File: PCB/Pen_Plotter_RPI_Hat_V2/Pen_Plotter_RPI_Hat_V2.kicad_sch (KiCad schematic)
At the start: 8 parts, among them U1 ATmega328P-P, Y1 X322516MLB4SI

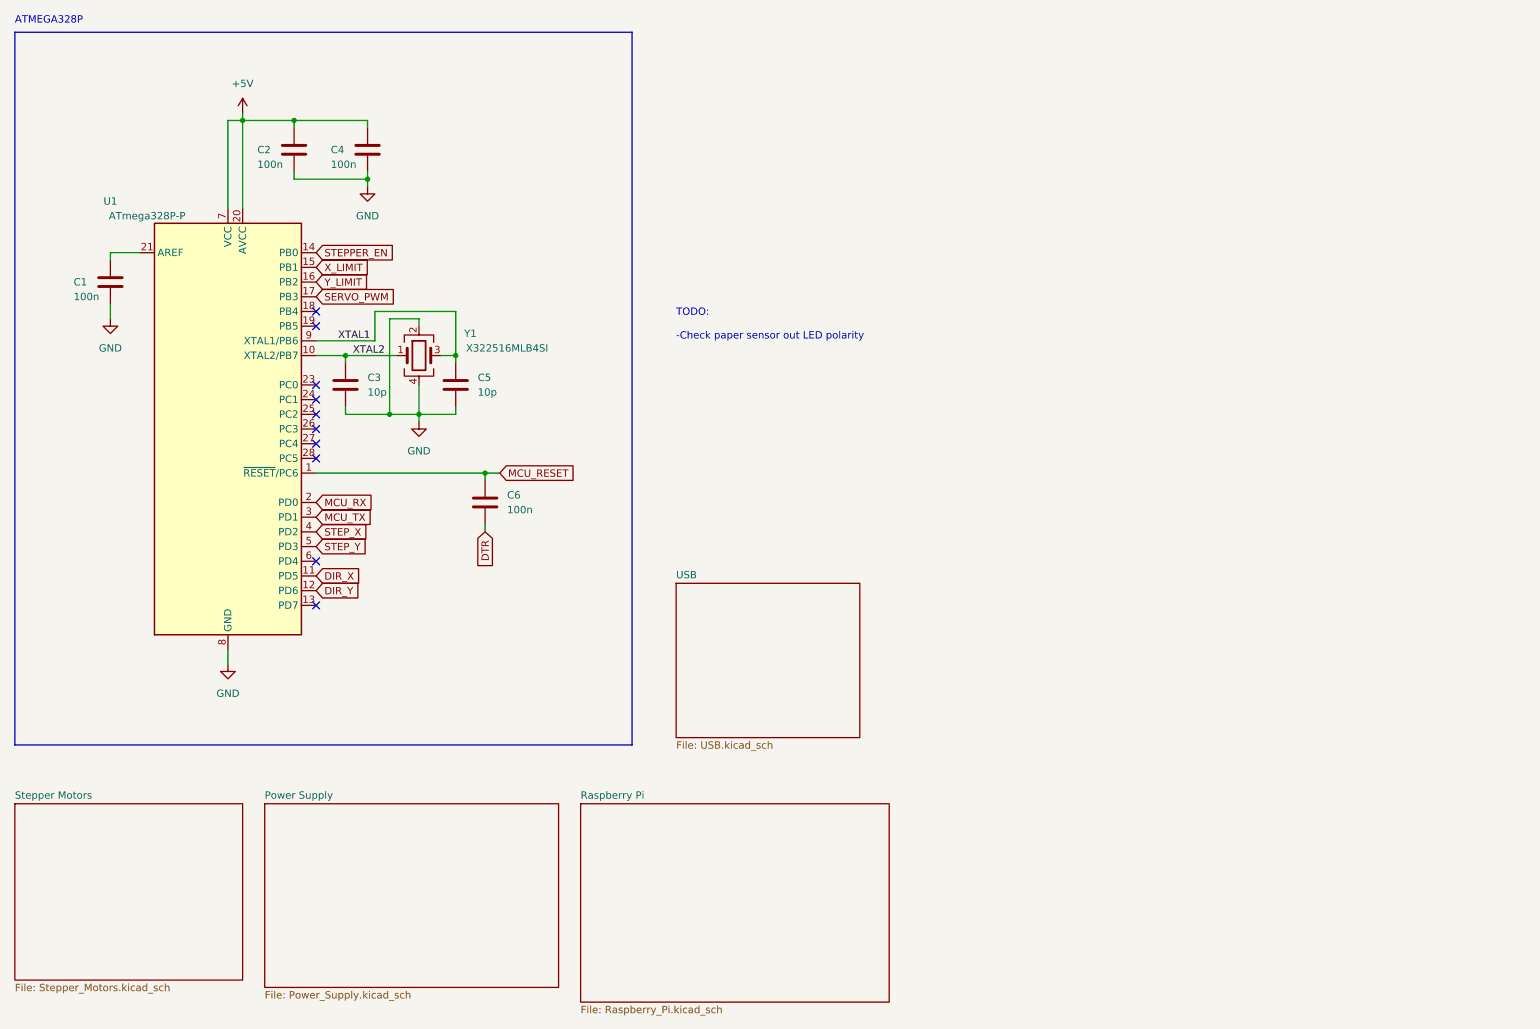
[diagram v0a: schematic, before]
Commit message: Simplified design, began layout process
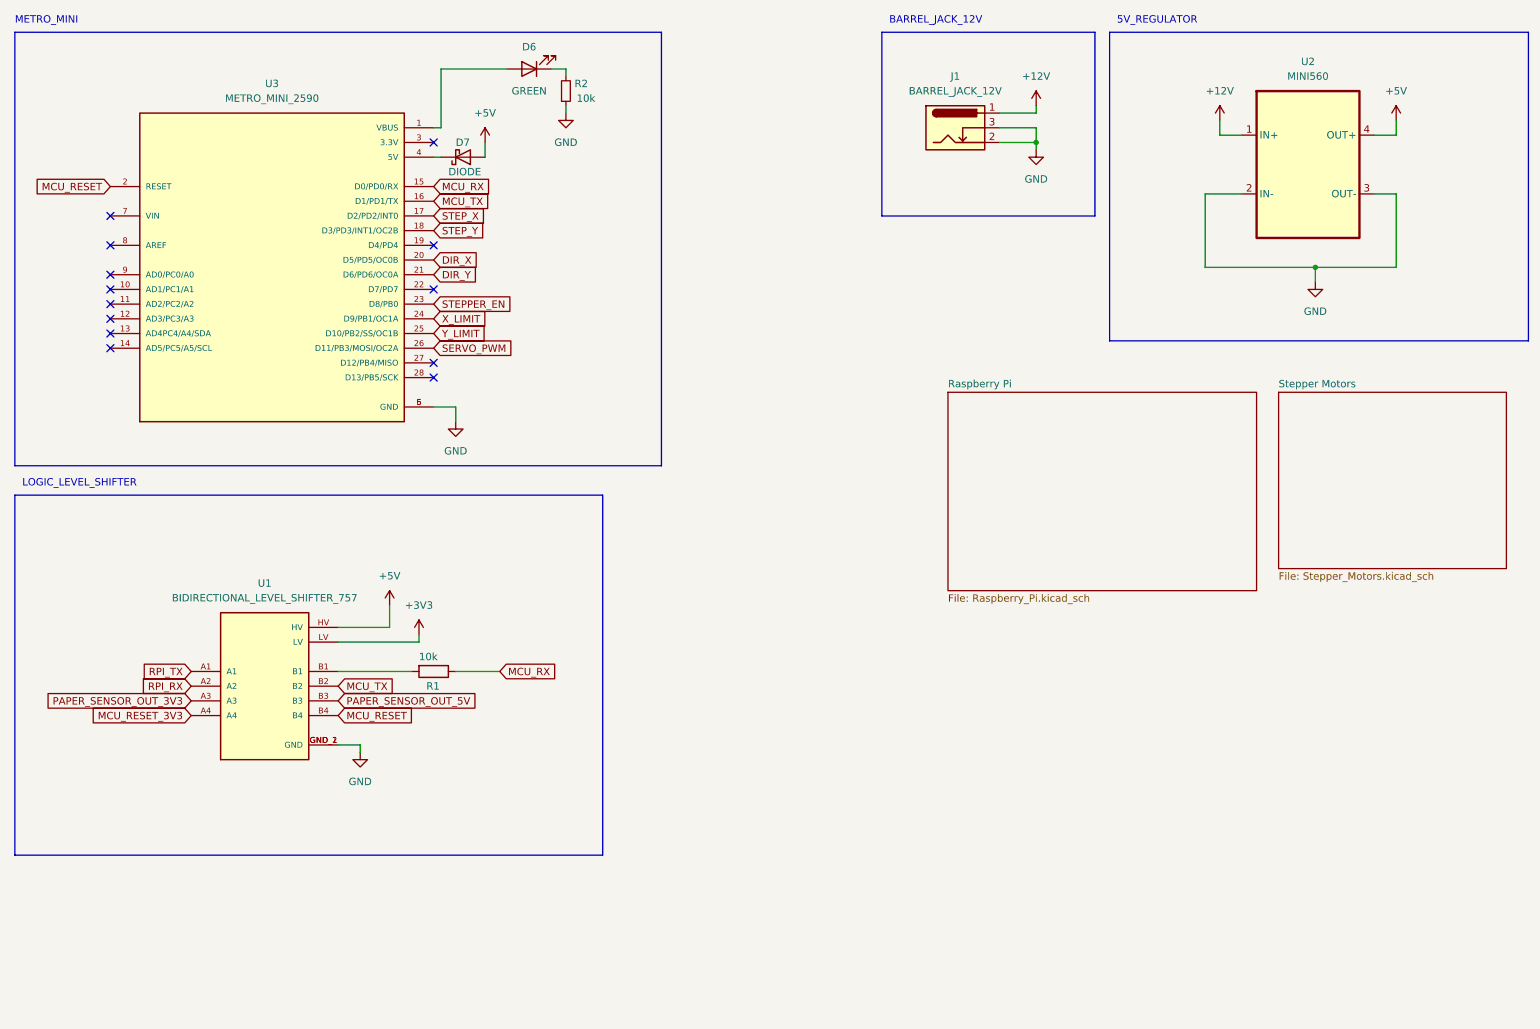
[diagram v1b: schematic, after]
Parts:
- removed C1, C2, C4, C6: 100n, Capacitor_SMD:C_0805_2012Metric, symbol Device:C
- removed C3, C5: 10p, Capacitor_SMD:C_0603_1608Metric, symbol Device:C
- removed U1: ATmega328P-P, Package_DIP:DIP-28_W7.62mm, symbol MCU_Microchip_ATmega:ATmega328P-P
- removed Y1: X322516MLB4SI, Crystal:Crystal_SMD_3225-4Pin_3.2x2.5mm, symbol Device:Crystal_GND24
- added D6: GREEN, LED_THT:LED_D5.0mm, symbol Device:LED
- added D7: DIODE, Diode_THT:D_5W_P10.16mm_Horizontal, symbol Device:D_Schottky
- added J1: BARREL_JACK_12V, Connector_BarrelJack:BarrelJack_Wuerth_6941xx301002, symbol Connector:Barrel_Jack_Switch
- added R1: 10k, Pen_Plotter_Lib:THT_RESISTOR_WITH_VALUE, symbol Device:R
- added R2: 10k, Pen_Plotter_Lib:THT_RESISTOR_WITH_VALUE, symbol Device:R_Small
- added U1: BIDIRECTIONAL_LEVEL_SHIFTER_757, Pen_Plotter_Lib:BIDIRECTIONAL_LEVEL_SHIFTER_575, symbol Pen_Plotter_Lib:BIDIRECTIONAL_LEVEL_SHIFTER_757
- added U2: MINI560, Pen_Plotter_Lib:MINI560_5V, symbol Pen_Plotter_Lib:MINI560
- added U3: METRO_MINI_2590, Pen_Plotter_Lib:METRO_MINI_MODULE_2590, symbol Pen_Plotter_Lib:METRO_MINI_2590
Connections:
- net +5V: now also D7.2 (A), U1.HV, U2.4 (OUT+)
- net DIR_X: now also U3.20 (D5/PD5/OC0B)
- net DIR_Y: now also U3.21 (D6/PD6/OC0A)
- net GND: now also J1.2, J1.3, R2.1, U1.GND_1 (GND), U1.GND_2 (GND), U2.2 (IN-), U2.3 (OUT-), U3.5 (GND), U3.6 (GND)
- net MCU_RESET: now also U1.B4, U3.2 (RESET)
- net MCU_RX: now also R1.1, U3.15 (D0/PD0/RX)
- net MCU_TX: now also U1.B2, U3.16 (D1/PD1/TX)
- net SERVO_PWM: now also U3.26 (D11/PB3/MOSI/OC2A)
- net STEPPER_EN: now also U3.23 (D8/PB0)
- net STEP_X: now also U3.17 (D2/PD2/INT0)
- net STEP_Y: now also U3.18 (D3/PD3/INT1/OC2B)
- net X_LIMIT: now also U3.24 (D9/PB1/OC1A)
- net Y_LIMIT: now also U3.25 (D10/PB2/SS/OC1B)
- new net: R1.2, U1.B1
- new net: D6.2 (A), U3.1 (VBUS)
- new net: D7.1 (K), U3.4 (5V)
- new net: D6.1 (K), R2.2
- new net +12V: J1.1, U2.1 (IN+)
- new net +3V3: U1.LV
- new net MCU_RESET_3V3: U1.A4
- new net PAPER_SENSOR_OUT_3V3: U1.A3
- new net PAPER_SENSOR_OUT_5V: U1.B3
- new net RPI_RX: U1.A2
- new net RPI_TX: U1.A1
- no-connect marks 10 -> 13
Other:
- removed sheet Power Supply
- removed sheet USB
- note added: "5V_REGULATOR"
- note added: "BARREL_JACK_12V"
- note added: "LOGIC_LEVEL_SHIFTER"
- note added: "METRO_MINI"
- note removed: "ATMEGA328P"
- note removed: "TODO: -Check paper sensor out LED polarity"

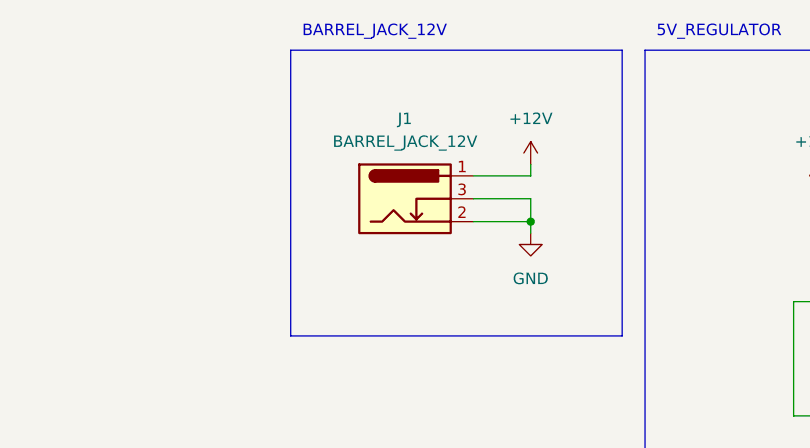
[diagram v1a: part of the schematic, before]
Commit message: Completed PCB layout, started routing
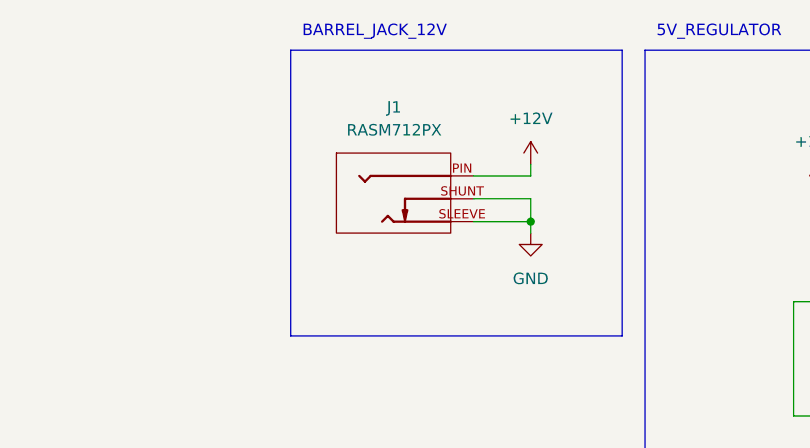
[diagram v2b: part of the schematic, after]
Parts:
- removed J1: BARREL_JACK_12V, Connector_BarrelJack:BarrelJack_Wuerth_6941xx301002, symbol Connector:Barrel_Jack_Switch
- added J1: RASM712PX, Pen_Plotter_Lib:SWITCHCRAFT_RASM712PX, symbol Pen_Plotter_Lib:RASM712PX
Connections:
- net +12V: now also J1.PIN
- net GND: now also J1.SHUNT, J1.SLEEVE
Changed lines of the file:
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@@
+    )
+  )
+  (symbol (lib_id "Pen_Plotter_Lib:RASM712PX") (at 181.61 39.37 0) (unit 1)
+    (in_bom yes) (on_board yes) (dnp no) (fields_autoplaced)
+    (property "Reference" "J1" (at 180.4035 29.21 0)
+      (effects (font (size 1.27 1.27)))
+    )
+    (property "Value" "RASM712PX" (at 180.4035 31.75 0)
+      (effects (font (size 1.27 1.27)))
+    )
+    (property "Footprint" "Pen_Plotter_Lib:SWITCHCRAFT_RASM712PX" (at 181.61 39.37 0)
+      (effects (font (size 1.27 1.27)) (justify bottom) hide)
+    )
+    (property "Datasheet" "" (at 181.61 39.37 0)
+      (effects (font (size 1.27 1.27)) hide)
+    )
+    (property "PARTREV" "A" (at 181.61 39.37 0)
+      (effects (font (size 1.27 1.27)) (justify bottom) hide)
+    )
+    (property "STANDARD" "Manufacturer Recommendations" (at 181.61 39.37 0)
+      (effects (font (size 1.27 1.27)) (justify bottom) hide)
+    )
+    (property "MAXIMUM_PACKAGE_HEIGHT" "11.11 mm" (at 181.61 39.37 0)
+      (effects (font (size 1.27 1.27)) (justify bottom) hide)
+    )
+    (property "MANUFACTURER" "Switchcraft" (at 181.61 39.37 0)
+      (effects (font (size 1.27 1.27)) (justify bottom) hide)
+    )
+    (pin "SLEEVE")
+    (pin "PIN")
+    (pin "SHUNT")
+    (instances
+      (project "Pen_Plotter_RPI_Hat_V2"
+        (path "/a2e71921-3692-4a11-8676-7b25cde44301"
+          (reference "J1") (unit 1)
+        )
+      )
     )
   )
@@
         )
       )
-    )
-  )
-  (symbol (lib_id "Connector:Barrel_Jack_Switch") (at 181.61 39.37 0) (unit 1)
-    (in_bom yes) (on_board yes) (dnp no) (fields_autoplaced)
-    (property "Reference" "J1" (at 181.61 30.48 0)
-      (effects (font (size 1.27 1.27)))
-    )
-    (property "Value" "BARREL_JACK_12V" (at 181.61 33.02 0)
-      (effects (font (size 1.27 1.27)))
-    )
-    (property "Footprint" "Connector_BarrelJack:BarrelJack_Wuerth_6941xx301002" (at 182.88 40.386 0)
-      (effects (font (size 1.27 1.27)) hide)
-    )
-    (property "Datasheet" "~" (at 182.88 40.386 0)
-      (effects (font (size 1.27 1.27)) hide)
-    )
-    (pin "1")
-    (pin "3")
-    (pin "2")
-    (instances
-      (project "Pen_Plotter_RPI_Hat_V2"
-        (path "/a2e71921-3692-4a11-8676-7b25cde44301"
-          (reference "J1") (unit 1)
-        )
-      )

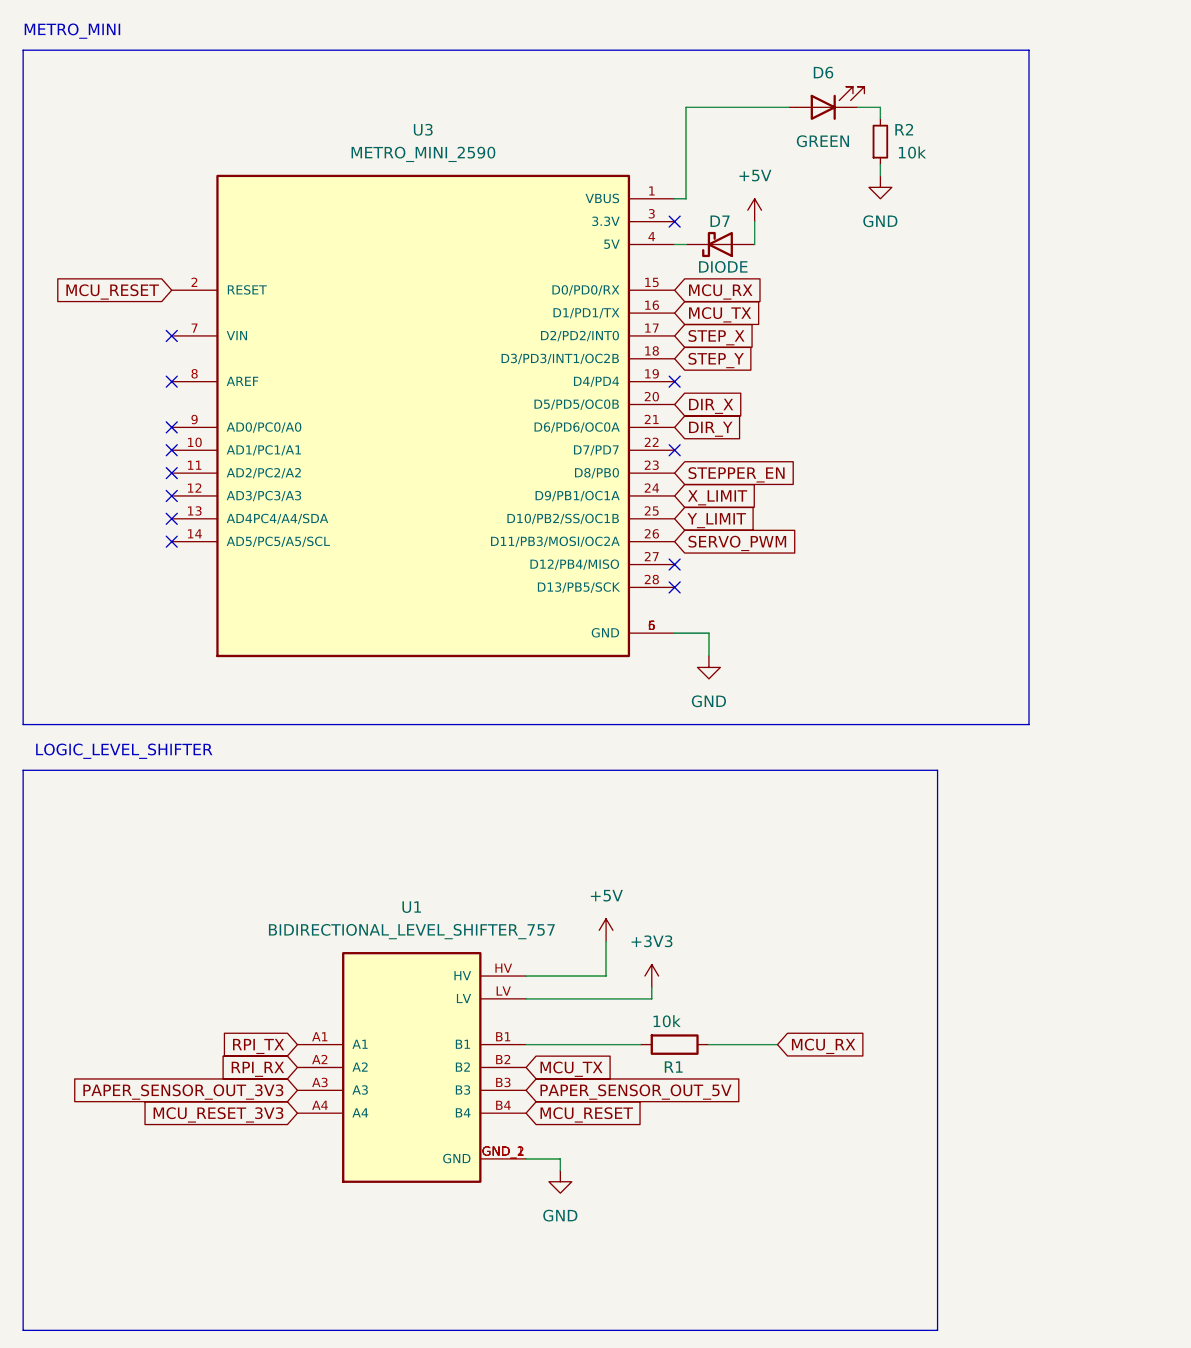
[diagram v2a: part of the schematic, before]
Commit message: Started work on converting to atmega328p control circuit
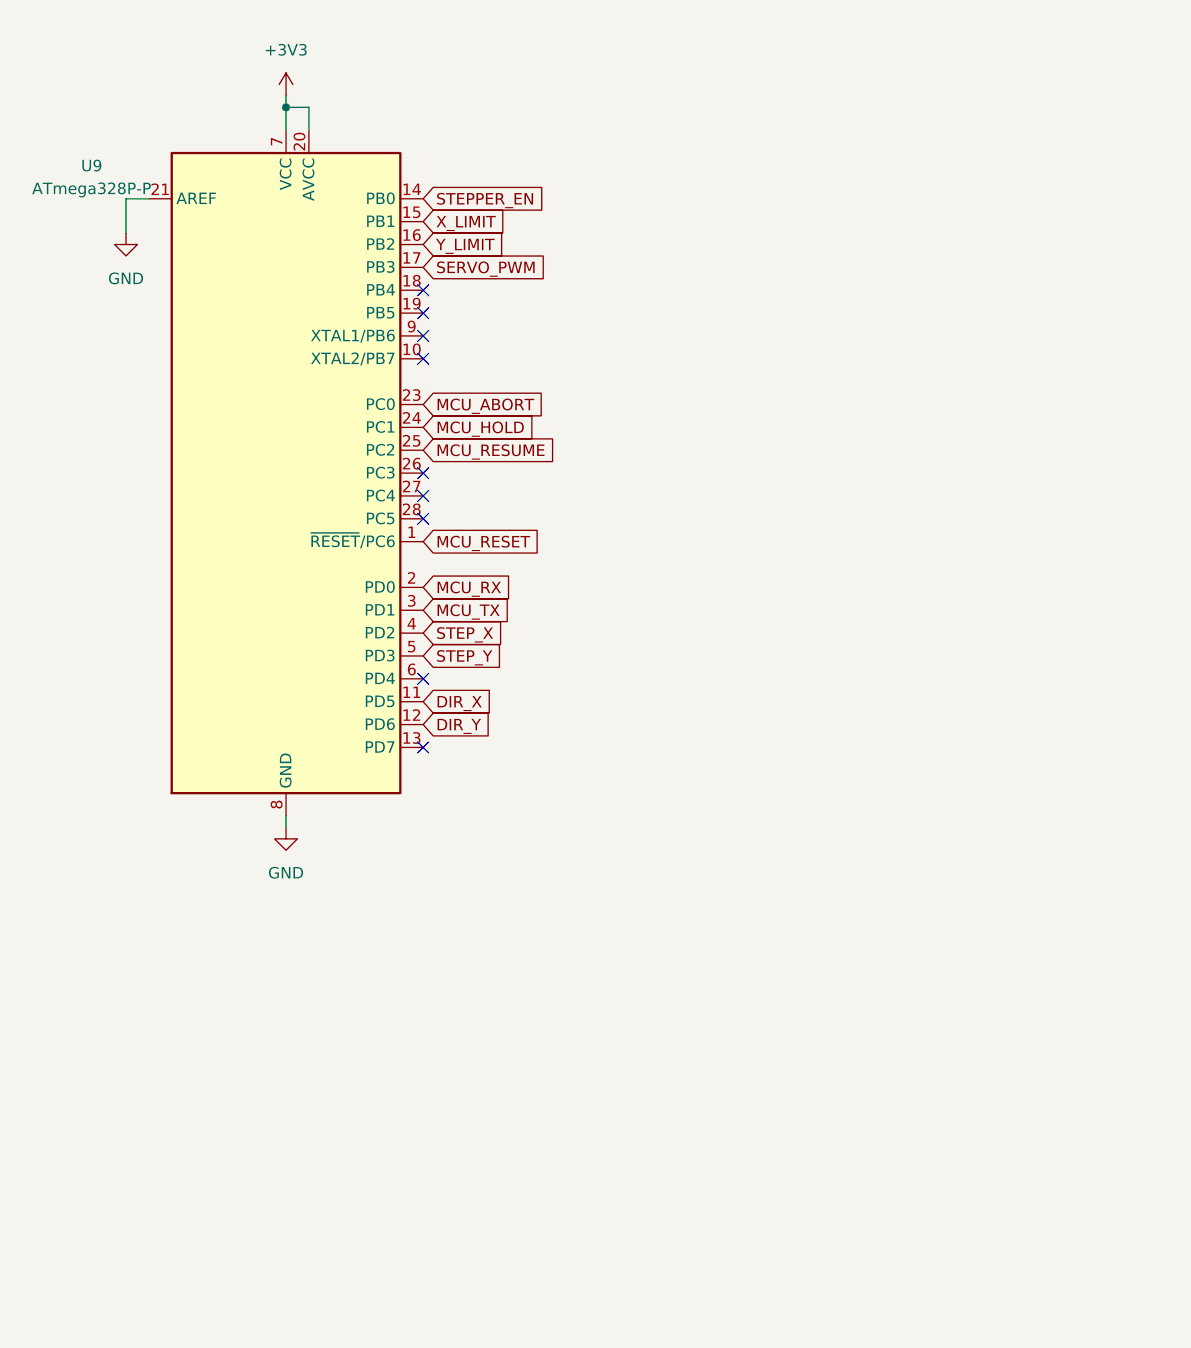
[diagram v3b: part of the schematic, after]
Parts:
- removed D6: GREEN, LED_THT:LED_D5.0mm, symbol Device:LED
- removed D7: DIODE, Diode_THT:D_5W_P10.16mm_Horizontal, symbol Device:D_Schottky
- removed R1: 10k, Pen_Plotter_Lib:THT_RESISTOR_WITH_VALUE, symbol Device:R
- removed R2: 10k, Pen_Plotter_Lib:THT_RESISTOR_WITH_VALUE, symbol Device:R_Small
- removed U1: BIDIRECTIONAL_LEVEL_SHIFTER_757, Pen_Plotter_Lib:BIDIRECTIONAL_LEVEL_SHIFTER_575, symbol Pen_Plotter_Lib:BIDIRECTIONAL_LEVEL_SHIFTER_757
- removed U3: METRO_MINI_2590, Pen_Plotter_Lib:METRO_MINI_MODULE_2590, symbol Pen_Plotter_Lib:METRO_MINI_2590
- added U9: ATmega328P-P, Package_DIP:DIP-28_W7.62mm, symbol MCU_Microchip_ATmega:ATmega328P-P
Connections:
- net +3V3: now also U9.20 (AVCC), U9.7 (VCC)
- net DIR_X: now also U9.11 (PD5)
- net DIR_Y: now also U9.12 (PD6)
- net GND: now also U9.21 (AREF), U9.22 (GND), U9.8 (GND)
- net MCU_RESET: now also U9.1 (~{RESET}/PC6)
- net MCU_RX: now also U9.2 (PD0)
- net MCU_TX: now also U9.3 (PD1)
- net SERVO_PWM: now also U9.17 (PB3)
- net STEPPER_EN: now also U9.14 (PB0)
- net STEP_X: now also U9.4 (PD2)
- net STEP_Y: now also U9.5 (PD3)
- net X_LIMIT: now also U9.15 (PB1)
- net Y_LIMIT: now also U9.16 (PB2)
- new net MCU_ABORT: U9.23 (PC0)
- new net MCU_HOLD: U9.24 (PC1)
- new net MCU_RESUME: U9.25 (PC2)
- no-connect marks 13 -> 9
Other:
- note removed: "LOGIC_LEVEL_SHIFTER"
- note removed: "METRO_MINI"

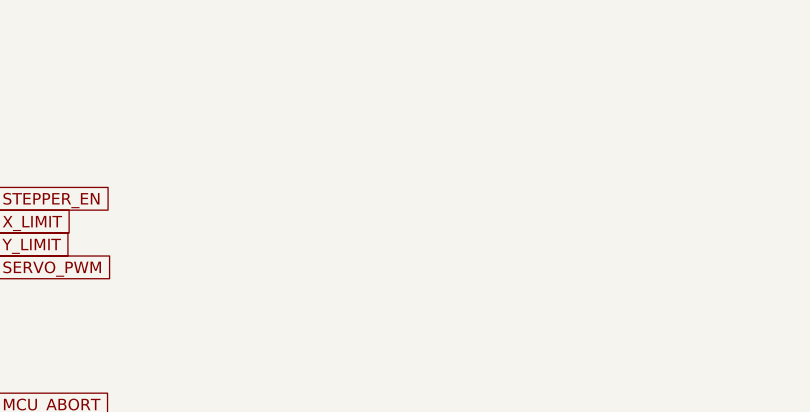
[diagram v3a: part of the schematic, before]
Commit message: Added third stepper motor driver
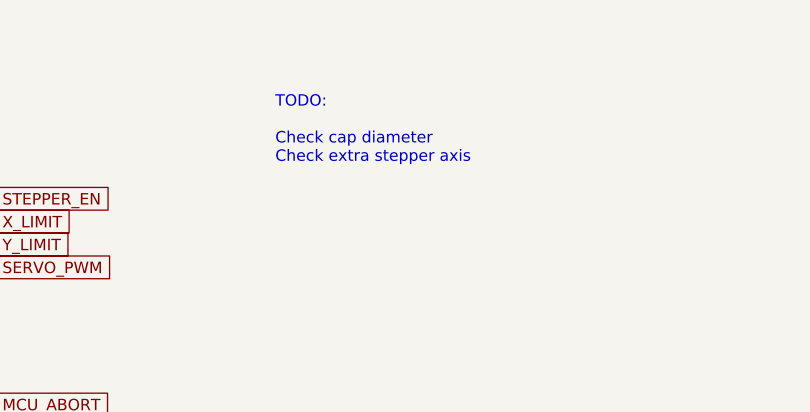
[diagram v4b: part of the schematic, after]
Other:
- note added: "TODO: Check cap diameter Check extra stepper axis"
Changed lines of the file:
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@@
+    (effects (font (size 1.27 1.27)) (justify left bottom))
+  )
+  (text "TODO:\n\nCheck cap diameter\nCheck extra stepper axis"
+    (at 95.25 35.56 0)
     (effects (font (size 1.27 1.27)) (justify left bottom))
   )
